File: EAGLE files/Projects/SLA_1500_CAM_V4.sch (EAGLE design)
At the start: 91 parts, among them J2 JST GH SM06B, J3 MOLEX 53261-03, J4 MOLEX 53261-04, J5 MOLEX 53261-04, J6 MOLEX 53261-04, U11 TXS0102, U2 TPS73633DCQR, U8 TXS0102, U9 TXS0102

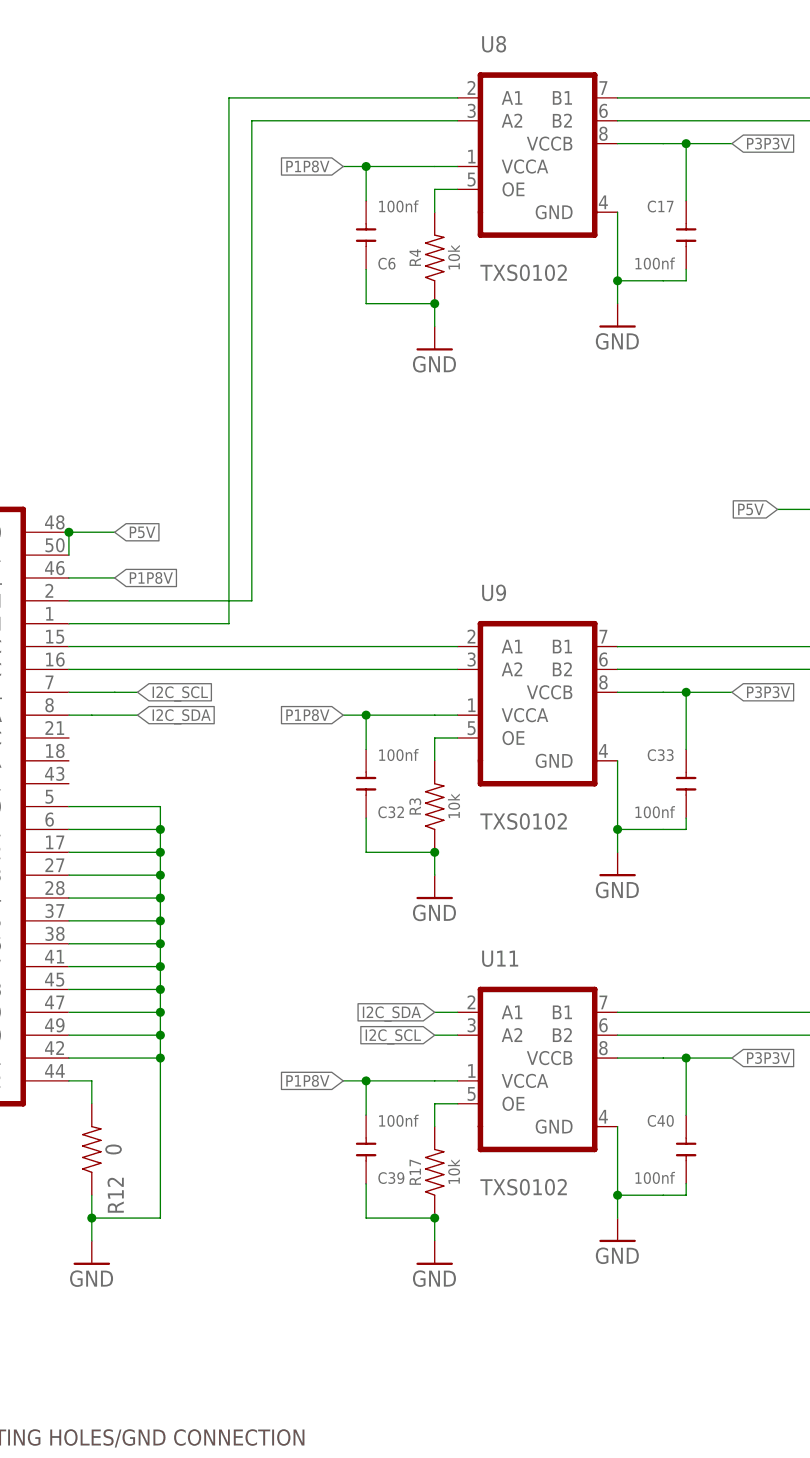
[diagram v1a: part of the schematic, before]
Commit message: Update SLA1500 CAM V4
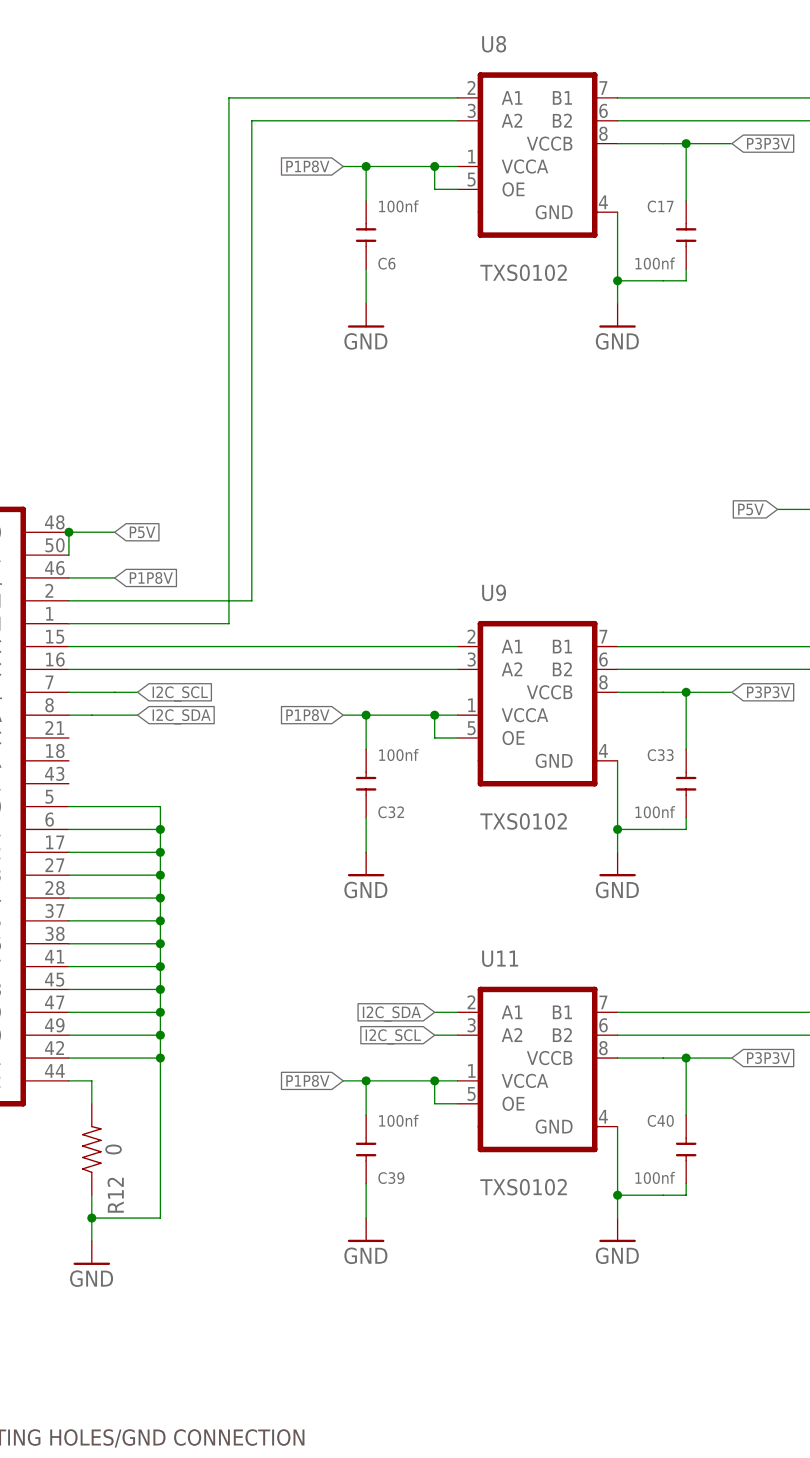
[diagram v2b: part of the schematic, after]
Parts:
- removed R17, R3, R4: 10k, SparkFun-Resistors:10KOHM-0603-1/10W-1%
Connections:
- removed net N$2: R3.2, U9.OE
- removed net N$3: R4.2, U8.OE
- removed net N$54: R17.2, U11.OE
- net GND: no longer R17.1, R3.1, R4.1
- net P1P8V: now also U11.OE, U8.OE, U9.OE
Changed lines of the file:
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@@
 <part name="C17" library="Seeed-Capacitor" library_urn="urn:adsk.eagle:library:464" deviceset="CERAMIC-100NF-25V-10%-X7R(0402)" device="" package3d_urn="urn:adsk.eagle:package:32379/1" value="100nf"/>
 <part name="GND40" library="supply1" library_urn="urn:adsk.eagle:library:371" deviceset="GND" device=""/>
-<part name="R4" library="SparkFun-Resistors" library_urn="urn:adsk.eagle:library:532" deviceset="10KOHM" device="-0603-1/10W-1%" package3d_urn="urn:adsk.eagle:package:39650/1" value="10k"/>
 <part name="GND41" library="supply1" library_urn="urn:adsk.eagle:library:371" deviceset="GND" device=""/>
 <part name="U8" library="Sightline" deviceset="TXS0102DQM" device="" value="TXS0102"/>
@@
 <part name="C33" library="Seeed-Capacitor" library_urn="urn:adsk.eagle:library:464" deviceset="CERAMIC-100NF-25V-10%-X7R(0402)" device="" package3d_urn="urn:adsk.eagle:package:32379/1" value="100nf"/>
 <part name="GND32" library="supply1" library_urn="urn:adsk.eagle:library:371" deviceset="GND" device=""/>
-<part name="R3" library="SparkFun-Resistors" library_urn="urn:adsk.eagle:library:532" deviceset="10KOHM" device="-0603-1/10W-1%" package3d_urn="urn:adsk.eagle:package:39650/1" value="10k"/>
 <part name="GND33" library="supply1" library_urn="urn:adsk.eagle:library:371" deviceset="GND" device=""/>
 <part name="U9" library="Sightline" deviceset="TXS0102DQM" device="" value="TXS0102"/>
@@
 <part name="C40" library="Seeed-Capacitor" library_urn="urn:adsk.eagle:library:464" deviceset="CERAMIC-100NF-25V-10%-X7R(0402)" device="" package3d_urn="urn:adsk.eagle:package:32379/1" value="100nf"/>
 <part name="GND38" library="supply1" library_urn="urn:adsk.eagle:library:371" deviceset="GND" device=""/>
-<part name="R17" library="SparkFun-Resistors" library_urn="urn:adsk.eagle:library:532" deviceset="10KOHM" device="-0603-1/10W-1%" package3d_urn="urn:adsk.eagle:package:39650/1" value="10k"/>
 <part name="GND39" library="supply1" library_urn="urn:adsk.eagle:library:371" deviceset="GND" device=""/>
 <part name="U11" library="Sightline" deviceset="TXS0102DQM" device="" value="TXS0102"/>
@@
 <attribute name="VALUE" x="337.82" y="180.34" size="1.778" layer="96"/>
 </instance>
-<instance part="R4" gate="G$1" x="320.04" y="190.5" smashed="yes" rot="R90">
-<attribute name="NAME" x="318.516" y="190.5" size="1.27" layer="95" font="vector" rot="R90" align="bottom-center"/>
-<attribute name="VALUE" x="321.564" y="190.5" size="1.27" layer="96" font="vector" rot="R90" align="top-center"/>
-</instance>
-<instance part="GND41" gate="1" x="320.04" y="180.34" smashed="yes">
-<attribute name="VALUE" x="317.5" y="177.8" size="1.778" layer="96"/>
+<instance part="GND41" gate="1" x="312.42" y="182.88" smashed="yes">
+<attribute name="VALUE" x="309.88" y="180.34" size="1.778" layer="96"/>
 </instance>
 <instance part="U8" gate="G$1" x="325.12" y="193.04" smashed="yes">
@@
 <attribute name="VALUE" x="337.82" y="119.38" size="1.778" layer="96"/>
 </instance>
-<instance part="R3" gate="G$1" x="320.04" y="129.54" smashed="yes" rot="R90">
-<attribute name="NAME" x="318.516" y="129.54" size="1.27" layer="95" font="vector" rot="R90" align="bottom-center"/>
-<attribute name="VALUE" x="321.564" y="129.54" size="1.27" layer="96" font="vector" rot="R90" align="top-center"/>
-</instance>
-<instance part="GND33" gate="1" x="320.04" y="119.38" smashed="yes">
-<attribute name="VALUE" x="317.5" y="116.84" size="1.778" layer="96"/>
+<instance part="GND33" gate="1" x="312.42" y="121.92" smashed="yes">
+<attribute name="VALUE" x="309.88" y="119.38" size="1.778" layer="96"/>
 </instance>
 <instance part="U9" gate="G$1" x="325.12" y="132.08" smashed="yes">
@@
 <attribute name="VALUE" x="337.82" y="78.74" size="1.778" layer="96"/>
 </instance>
-<instance part="R17" gate="G$1" x="320.04" y="88.9" smashed="yes" rot="R90">
-<attribute name="NAME" x="318.516" y="88.9" size="1.27" layer="95" font="vector" rot="R90" align="bottom-center"/>
-<attribute name="VALUE" x="321.564" y="88.9" size="1.27" layer="96" font="vector" rot="R90" align="top-center"/>
-</instance>
-<instance part="GND39" gate="1" x="320.04" y="78.74" smashed="yes">
-<attribute name="VALUE" x="317.5" y="76.2" size="1.778" layer="96"/>
+<instance part="GND39" gate="1" x="312.42" y="81.28" smashed="yes">
+<attribute name="VALUE" x="309.88" y="78.74" size="1.778" layer="96"/>
 </instance>
 <instance part="U11" gate="G$1" x="325.12" y="91.44" smashed="yes">
@@
 </segment>
 <segment>
-<pinref part="GND41" gate="1" pin="GND"/>
-<pinref part="R4" gate="G$1" pin="1"/>
-<wire x1="320.04" y1="182.88" x2="320.04" y2="185.42" width="0.1524" layer="91"/>
-<pinref part="C6" gate="G$1" pin="1"/>
-<wire x1="312.42" y1="189.23" x2="312.42" y2="185.42" width="0.1524" layer="91"/>
-<wire x1="312.42" y1="185.42" x2="320.04" y2="185.42" width="0.1524" layer="91"/>
-<junction x="320.04" y="185.42"/>
-</segment>
-<segment>
 <pinref part="GND45" gate="1" pin="GND"/>
 <pinref part="C38" gate="G$1" pin="-"/>
@@
 </segment>
 <segment>
-<pinref part="GND33" gate="1" pin="GND"/>
-<pinref part="R3" gate="G$1" pin="1"/>
-<wire x1="320.04" y1="121.92" x2="320.04" y2="124.46" width="0.1524" layer="91"/>
-<pinref part="C32" gate="G$1" pin="1"/>
-<wire x1="312.42" y1="128.27" x2="312.42" y2="124.46" width="0.1524" layer="91"/>
-<wire x1="312.42" y1="124.46" x2="320.04" y2="124.46" width="0.1524" layer="91"/>
-<junction x="320.04" y="124.46"/>
-</segment>
-<segment>
 <pinref part="GND38" gate="1" pin="GND"/>
 <wire x1="340.36" y1="83.82" x2="340.36" y2="86.36" width="0.1524" layer="91"/>
@@
 <wire x1="345.44" y1="86.36" x2="340.36" y2="86.36" width="0.1524" layer="91"/>
 <junction x="340.36" y="86.36"/>
-</segment>
-<segment>
-<pinref part="GND39" gate="1" pin="GND"/>
-<pinref part="R17" gate="G$1" pin="1"/>
-<wire x1="320.04" y1="81.28" x2="320.04" y2="83.82" width="0.1524" layer="91"/>
-<pinref part="C39" gate="G$1" pin="1"/>
-<wire x1="312.42" y1="87.63" x2="312.42" y2="83.82" width="0.1524" layer="91"/>
-<wire x1="312.42" y1="83.82" x2="320.04" y2="83.82" width="0.1524" layer="91"/>
-<junction x="320.04" y="83.82"/>
 </segment>
 <segment>
@@
 <wire x1="381.00125" y1="137.16" x2="378.46125" y2="137.1371875" width="0.1524" layer="91"/>
 </segment>
+<segment>
+<pinref part="GND41" gate="1" pin="GND"/>
+<pinref part="C6" gate="G$1" pin="1"/>
+<wire x1="312.42" y1="185.42" x2="312.42" y2="189.23" width="0.1524" layer="91"/>
+</segment>
+<segment>
+<pinref part="GND33" gate="1" pin="GND"/>
+<pinref part="C32" gate="G$1" pin="1"/>
+<wire x1="312.42" y1="124.46" x2="312.42" y2="128.27" width="0.1524" layer="91"/>
+</segment>
+<segment>
+<pinref part="GND39" gate="1" pin="GND"/>
+<pinref part="C39" gate="G$1" pin="1"/>
+<wire x1="312.42" y1="83.82" x2="312.42" y2="87.63" width="0.1524" layer="91"/>
+</segment>
 </net>
 <net name="I2C_SCL" class="0">
@@
 <wire x1="312.42" y1="196.85" x2="312.42" y2="200.66" width="0.1524" layer="91"/>
 <junction x="312.42" y="200.66"/>
+<pinref part="U8" gate="G$1" pin="OE"/>
+<wire x1="322.58" y1="198.12" x2="320.04" y2="198.12" width="0.1524" layer="91"/>
+<wire x1="320.04" y1="198.12" x2="320.04" y2="200.66" width="0.1524" layer="91"/>
+<junction x="320.04" y="200.66"/>
 </segment>
 <segment>
@@
 <wire x1="312.42" y1="135.89" x2="312.42" y2="139.7" width="0.1524" layer="91"/>
 <junction x="312.42" y="139.7"/>
+<pinref part="U9" gate="G$1" pin="OE"/>
+<wire x1="322.58" y1="137.16" x2="320.04" y2="137.16" width="0.1524" layer="91"/>
+<wire x1="320.04" y1="137.16" x2="320.04" y2="139.7" width="0.1524" layer="91"/>
+<junction x="320.04" y="139.7"/>
 </segment>
 <segment>
@@
 <wire x1="312.42" y1="95.25" x2="312.42" y2="99.06" width="0.1524" layer="91"/>
 <junction x="312.42" y="99.06"/>
+<pinref part="U11" gate="G$1" pin="OE"/>
+<wire x1="322.58" y1="96.52" x2="320.04" y2="96.52" width="0.1524" layer="91"/>
+<wire x1="320.04" y1="96.52" x2="320.04" y2="99.06" width="0.1524" layer="91"/>
+<junction x="320.04" y="99.06"/>
 </segment>
 <segment>
@@
 </segment>
 </net>
-<net name="N$2" class="0">
-<segment>
-<pinref part="R3" gate="G$1" pin="2"/>
-<wire x1="320.04" y1="134.62" x2="320.04" y2="137.16" width="0.1524" layer="91"/>
-<wire x1="320.04" y1="137.16" x2="322.58" y2="137.16" width="0.1524" layer="91"/>
-<pinref part="U9" gate="G$1" pin="OE"/>
-</segment>
-</net>
 <net name="N$35" class="0">
 <segment>
@@
 </segment>
 </net>
-<net name="N$54" class="0">
-<segment>
-<pinref part="R17" gate="G$1" pin="2"/>
-<wire x1="320.04" y1="93.98" x2="320.04" y2="96.52" width="0.1524" layer="91"/>
-<wire x1="320.04" y1="96.52" x2="322.58" y2="96.52" width="0.1524" layer="91"/>
-<pinref part="U11" gate="G$1" pin="OE"/>
-</segment>
-</net>
 <net name="N$37" class="0">
 <segment>
@@
 </segment>
 </net>
-<net name="N$3" class="0">
-<segment>
-<pinref part="R4" gate="G$1" pin="2"/>
-<wire x1="320.04" y1="195.58" x2="320.04" y2="198.12" width="0.1524" layer="91"/>
-<pinref part="U8" gate="G$1" pin="OE"/>
-<wire x1="320.04" y1="198.12" x2="322.58" y2="198.12" width="0.1524" layer="91"/>
-</segment>
-</net>
